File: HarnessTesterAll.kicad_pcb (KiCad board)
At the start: 2 copper layers, 81 parts, among them J1 I/O B, J2 I/O A, J3 Power, J4 SWD, J5 Micro_SD_Card, J7 Boot, SW1 SW_MEC_5G, SW2 RoterySwitch, U1 STM32F103RETx, U2 5v regulator, U3 3.3v Regulator, U4 MAX232, U5 TXB0108, U6 TXB0108

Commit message: Started from scratch, Finished new schematic
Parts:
- removed ?: , 
- removed C1, C22, C23: 10uf, Resistor_SMD:R_0603_1608Metric
- removed C10, C11, C12, C13, C14, C15, C16, C17, C18, C19, C2, C20, C21, C3, C4, C5: 100uf, Resistor_SMD:R_0603_1608Metric
- removed C6, C7, C8, C9: 1uf, Resistor_SMD:R_0603_1608Metric
- removed D1, D2: LED, LED_SMD:LED_0201_0603Metric
- removed DS1: LCD, Display:WC1602A
- removed J1: I/O B, Connector_Molex:Molex_Mini-Fit_Jr_5569-12A2_2x06_P4.20mm_Horizontal
- removed J2: I/O A, Connector_Molex:Molex_Mini-Fit_Jr_5569-12A2_2x06_P4.20mm_Horizontal
- removed J3: Power, Connector_Molex:Molex_Mini-Fit_Jr_5569-04A2_2x02_P4.20mm_Horizontal
- removed J4: SWD, Connector_PinHeader_2.00mm:PinHeader_1x04_P2.00mm_Vertical
- removed J5: Micro_SD_Card, DM3D:DM3DSF
- removed J7: Boot, Connector_PinHeader_1.00mm:PinHeader_1x03_P1.00mm_Vertical
- removed LS2: CMI-9605IC-0380T, CMI-9605IC-0380T:CUI_CMI-9605IC-0380T
- removed R1, R10, R11, R12, R13, R14, R15, R16, R17, R18, R19, R2, R20, R21, R22, R23, R24, R25, R26, R27, R28, R29, R30, R31, R32, R33, R34, R35, R36, R37, R38, R39, R4: 10k, Resistor_SMD:R_0603_1608Metric
- removed R5, R6, R9: 470, Resistor_SMD:R_0603_1608Metric
- removed REF** (x3): MountingHole_4.3mm_M4, MountingHole:MountingHole_4.3mm_M4
- removed SW1: SW_MEC_5G, Button_Switch_SMD:SW_MEC_5GSH9
- removed SW2: RoterySwitch, Encoder:PEC11R4220FS0024
- removed U1: STM32F103RETx, Package_QFP:LQFP-64_10x10mm_P0.5mm
- removed U2: 5v regulator, TLE42744DV50ATMA1:DPAK229P994X241-3N
- removed U3: 3.3v Regulator, Package_TO_SOT_SMD:SOT-23
- removed U4: MAX232, Max232:SOIC127P1032X265-16N
- removed U5, U6: TXB0108, TXB0108PWR:SOP65P640X120-20N
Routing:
- net +3.3V: track 293.0 -> 0.00 mm, vias 6 -> 0
- net In3: track 199.5 -> 0.00 mm, vias 1 -> 0
- net In4: track 145.9 -> 0.00 mm, vias 1 -> 0
- net In2: track 140.4 -> 0.00 mm, vias 1 -> 0
- net In8: track 136.1 -> 0.00 mm, vias 1 -> 0
- net GND: track 136.0 -> 0.00 mm, vias 7 -> 0
- net In5: track 132.2 -> 0.00 mm, vias 1 -> 0
- net In1: track 128.9 -> 0.00 mm, vias 1 -> 0
- net In6: track 118.0 -> 0.00 mm, vias 1 -> 0
- net +5V: track 111.9 -> 0.00 mm, vias 4 -> 0
- net In7: track 99.6 -> 0.00 mm, vias 1 -> 0
- net Out6: track 92.7 -> 0.00 mm, vias 1 -> 0
- net In11: track 92.3 -> 0.00 mm, vias 3 -> 0
- net In12: track 88.7 -> 0.00 mm, vias 2 -> 0
- net In10: track 85.1 -> 0.00 mm, vias 2 -> 0
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- removed copper zone on B.Cu, net +5V
- removed copper zone on F.Cu, net GND

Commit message: Made a board laylout
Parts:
- added C1: 10uf, Capacitor_SMD:C_0603_1608Metric, F.Cu at (111.0, 113.0)
- added C2: 0.1uf, Capacitor_SMD:C_0603_1608Metric, F.Cu at (126.5, 111.5)
- added C3: 0.1uf, Capacitor_SMD:C_0603_1608Metric, F.Cu at (118.6, 119.9)
- added C4: 0.1uf, Capacitor_SMD:C_0603_1608Metric, F.Cu at (118.6, 104.4)
- added D1: LED, LED_SMD:LED_0603_1608Metric, F.Cu at (89.2, 93.3)
- added D2: LED, LED_SMD:LED_0603_1608Metric, F.Cu at (89.2, 95.1)
- added J1: Input Tester, Molex_2x6:CON_874271202, F.Cu at (102.7, 87.3)
- added J2: Output Tester, Molex_2x6:CON_874271202, F.Cu at (102.8, 122.4)
- added J3: JTAG, Connector_PinHeader_1.27mm:PinHeader_2x10_P1.27mm_Vertical, F.Cu at (138.7, 105.7)
- added R1: 10k, Resistor_SMD:R_0603_1608Metric, B.Cu at (96.0, 127.4)
- added R10: 10k, Resistor_SMD:R_0603_1608Metric, B.Cu at (96.1, 107.3)
- added R11: 10k, Resistor_SMD:R_0603_1608Metric, B.Cu at (95.9, 102.0)
- added R12: 10k, Resistor_SMD:R_0603_1608Metric, B.Cu at (95.8, 96.6)
- added R13: 10k, Resistor_SMD:R_0603_1608Metric, B.Cu at (95.7, 90.8)
- added R14: 10k, Resistor_SMD:R_0603_1608Metric, B.Cu at (95.7, 85.0)
- added R15: 10k, Resistor_SMD:R_0603_1608Metric, B.Cu at (95.7, 79.4)
- added R16: 10k, Resistor_SMD:R_0603_1608Metric, B.Cu at (96.1, 73.8)
- added R17: 10k, Resistor_SMD:R_0603_1608Metric, B.Cu at (96.2, 67.7)
- added R18: 10k, Resistor_SMD:R_0603_1608Metric, B.Cu at (96.2, 61.6)
- added R19: 10k, Resistor_SMD:R_0603_1608Metric, B.Cu at (95.7, 88.0)
- added R2: 10k, Resistor_SMD:R_0603_1608Metric, B.Cu at (96.0, 121.5)
- added R20: 10k, Resistor_SMD:R_0603_1608Metric, B.Cu at (95.7, 82.2)
- added R21: 10k, Resistor_SMD:R_0603_1608Metric, B.Cu at (95.8, 76.6)
- added R22: 10k, Resistor_SMD:R_0603_1608Metric, B.Cu at (96.0, 70.7)
- added R23: 10k, Resistor_SMD:R_0603_1608Metric, B.Cu at (96.2, 64.6)
- added R24: 10k, Resistor_SMD:R_0603_1608Metric, B.Cu at (96.2, 58.8)
- added R25: 10k, Resistor_SMD:R_0603_1608Metric, F.Cu at (92.4, 95.1)
- added R26: 10k, Resistor_SMD:R_0603_1608Metric, F.Cu at (92.4, 93.3)
- added R27: 10k, Resistor_SMD:R_0603_1608Metric, B.Cu at (118.9, 115.1)
- added R3: 10k, Resistor_SMD:R_0603_1608Metric, B.Cu at (96.0, 116.0)
- added R4: 10k, Resistor_SMD:R_0603_1608Metric, B.Cu at (96.0, 110.4)
- added R5: 10k, Resistor_SMD:R_0603_1608Metric, B.Cu at (96.0, 104.8)
- added R6: 10k, Resistor_SMD:R_0603_1608Metric, B.Cu at (95.8, 99.2)
- added R7: 10k, Resistor_SMD:R_0603_1608Metric, B.Cu at (96.0, 124.6)
- added R8: 10k, Resistor_SMD:R_0603_1608Metric, B.Cu at (96.0, 118.7)
- added R9: 10k, Resistor_SMD:R_0603_1608Metric, B.Cu at (96.0, 113.2)
- added SW1: Reset, Button_Switch_SMD:SW_MEC_5GSH9, F.Cu at (132.1, 69.6)
- added U1: PIC32MX110F016D-IPT, Package_QFP:TQFP-44_10x10mm_P0.8mm, F.Cu at (118.9, 112.2)
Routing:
- net In12: track 0.00 -> 94.6 mm
- net In11: track 0.00 -> 86.3 mm
- net In10: track 0.00 -> 77.6 mm
- net In6: track 0.00 -> 76.7 mm
- net RST: track 0.00 -> 69.7 mm, vias 0 -> 1
- net In9: track 0.00 -> 69.4 mm
- net In5: track 0.00 -> 69.3 mm
- net In8: track 0.00 -> 64.7 mm
- net In7: track 0.00 -> 60.9 mm
- net In4: track 0.00 -> 58.1 mm
- net In3: track 0.00 -> 52.1 mm
- net Out6: track 0.00 -> 45.1 mm
- net In2: track 0.00 -> 44.6 mm
- net Out5: track 0.00 -> 40.5 mm
- net In1: track 0.00 -> 38.2 mm
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- added copper zone on B.Cu, net +3.3V
- added copper zone on F.Cu, net GND

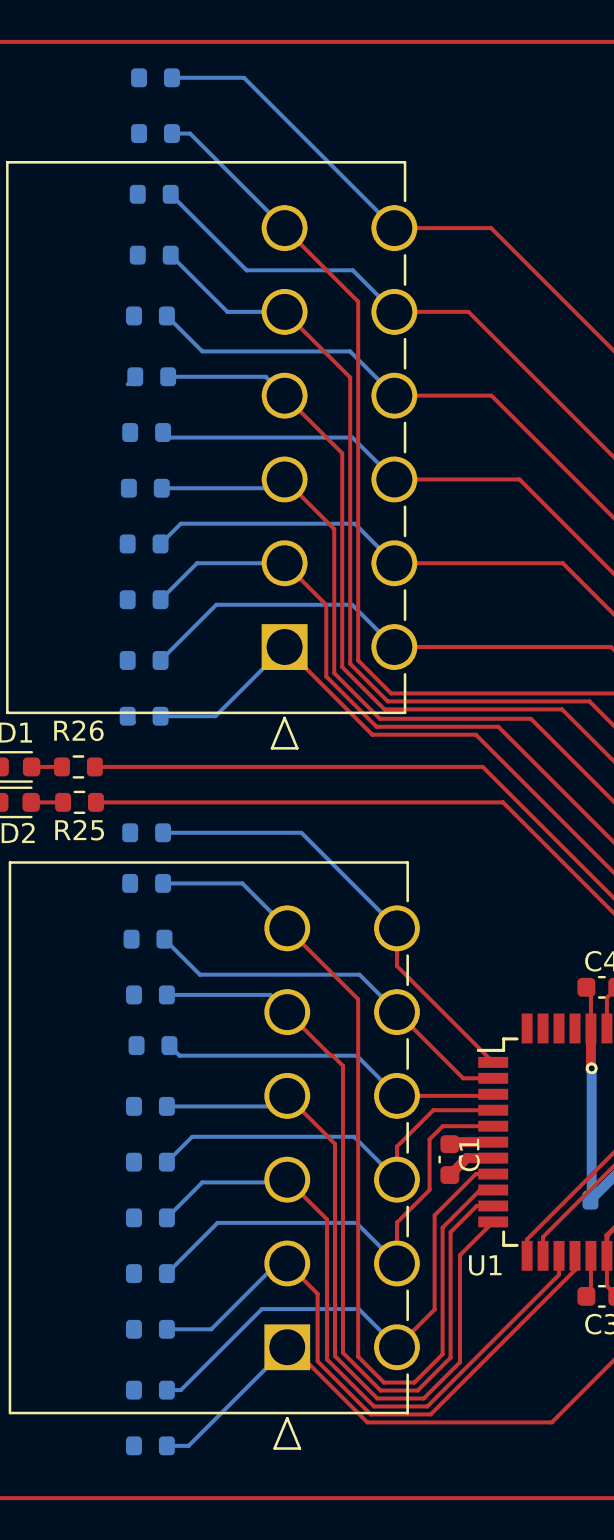
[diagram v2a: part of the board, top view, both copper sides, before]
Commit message: Added more clearense and moved pull up resistors
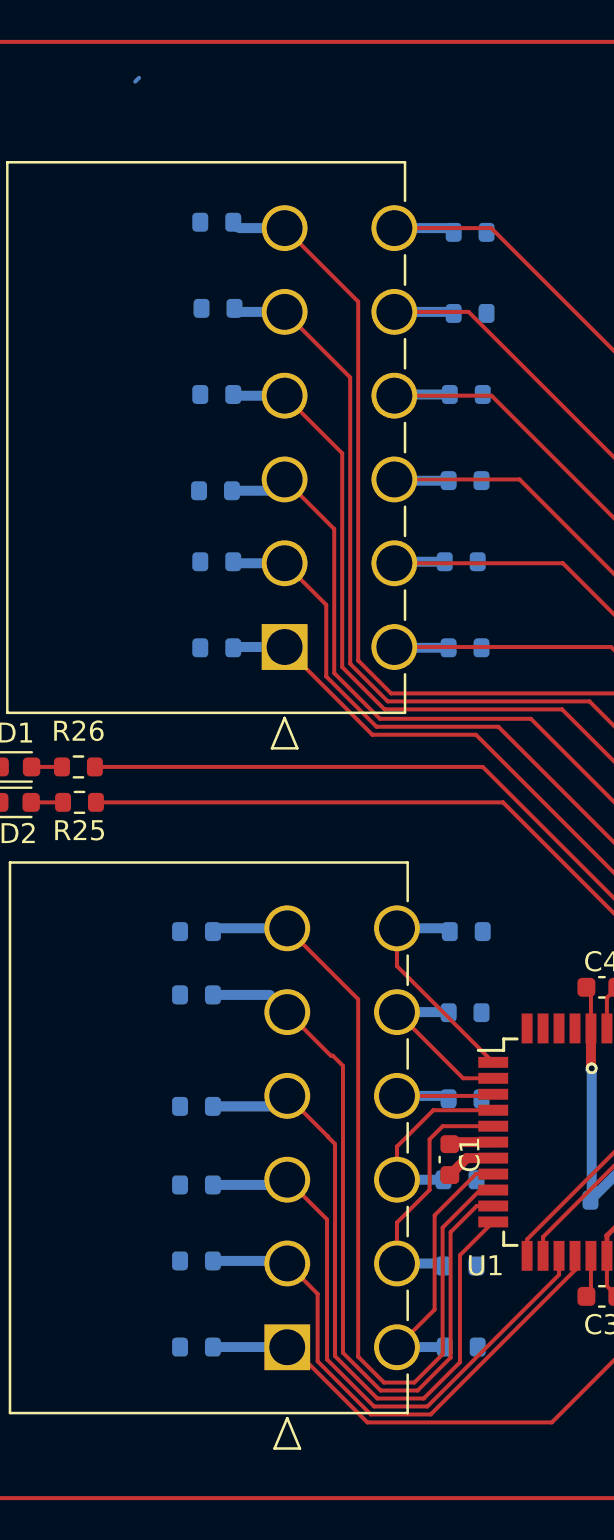
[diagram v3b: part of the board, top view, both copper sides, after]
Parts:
- moved R24 17.6 mm to (112.0, 66.5), turned to 180 degrees
- moved R23 16.9 mm to (112.0, 70.6), turned to 180 degrees
- moved R12 16.8 mm to (111.8, 101.6), turned to 180 degrees
- moved R22 16.3 mm to (111.8, 74.7), turned to 180 degrees
- moved R11 16.3 mm to (111.8, 105.7), turned to 180 degrees
- moved R21 16.1 mm to (111.8, 79.0), turned to 180 degrees
- moved R19 16.1 mm to (111.8, 87.4), turned to 180 degrees
- moved R20 15.9 mm to (111.6, 83.1), turned to 180 degrees
- moved R10 15.9 mm to (111.8, 110.0), turned to 180 degrees
- moved R7 15.7 mm to (111.6, 122.4), turned to 180 degrees
- moved R9 15.5 mm to (111.5, 114.0), turned to 180 degrees
- moved R8 15.5 mm to (111.5, 118.4), turned to 180 degrees
- moved R1 5.46 mm to (98.3, 122.4)
- moved R18 5.40 mm to (99.3, 66.0)
- moved R13 5.00 mm to (99.3, 87.4)
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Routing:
- net Out7: track 25.2 -> 13.6 mm
- net In12: track 94.6 -> 83.4 mm
- net Out8: track 23.8 -> 12.7 mm
- net In7: track 60.9 -> 49.9 mm
- net Out12: track 22.5 -> 11.5 mm
- net In11: track 86.3 -> 75.7 mm
- net Out9: track 20.2 -> 9.61 mm
- net Out11: track 19.4 -> 8.80 mm
- net In8: track 64.7 -> 54.3 mm
- net In10: track 77.6 -> 67.3 mm
- net In9: track 69.4 -> 59.5 mm
- net Out10: track 17.6 -> 7.80 mm
- net In1: track 38.2 -> 33.1 mm
- net In6: track 76.7 -> 71.8 mm
- net In2: track 44.6 -> 40.3 mm
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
